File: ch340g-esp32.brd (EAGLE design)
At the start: 100 x 80 mm, 0 parts

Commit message: rev1
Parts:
- added C1, C2: 22, rcl:C0805
- added C3, C5: 0.1uF, rcl:C0805
- added C4: 10uF, rcl:B/3528-21W
- added D1: YELLOW, 597-5311-402F:LEDC2012X70N
- added D2: GREEN, 597-5311-402F:LEDC2012X70N
- added IC1: (no value), lm1117:SOT223
- added JP1: OUT, pinhead:1X06
- added Q1: 12M, crystal:HC49/S
- added R1, R2: 10K, rcl:R0805
- added R3, R4: 2K, rcl:R0805
- added T1, T2: BC847, transistor:SOT23
- added U$1: MICRO-USB, microusb:MICRO-USB
- added U$2: CH340G, ch340g:SOIC16
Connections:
- new net +5V: C3.1, IC1.3, U$1.1
- new net D+: U$1.3, U$2.5
- new net D-: U$1.2, U$2.6
- new net DTR: R1.1, T2.2, U$2.13
- new net EN: JP1.1, T1.3
- new net GND: C1.2, C2.2, C3.2, C4.-, C5.2, IC1.1, JP1.6, U$1.5, U$1.GND1, U$1.GND2, U$2.1
- new net IO0: JP1.2, T2.3
- new net N$1: C2.1, Q1.2, U$2.8
- new net N$12: D2.A, R4.1
- new net N$2: C1.1, Q1.1, U$2.7
- new net N$3: R1.2, T1.1
- new net N$4: R2.2, T2.1
- new net N$5: D1.A, R3.1
- new net RTS: R2.1, T1.2, U$2.14
- new net RX: D2.C, JP1.3, U$2.3
- new net TX: D1.C, JP1.4, U$2.2
- new net VCC: C4.+, C5.1, IC1.2, IC1.TAB, JP1.5, R3.2, R4.2, U$2.16, U$2.4
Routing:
- net GND: track 0.00 -> 113.3 mm, vias 0 -> 6
- net VCC: track 0.00 -> 64.0 mm, vias 0 -> 2
- net TX: track 0.00 -> 31.7 mm, vias 0 -> 1
- net RX: track 0.00 -> 25.2 mm
- net D+: track 0.00 -> 17.7 mm
- net RTS: track 0.00 -> 15.7 mm
- net D-: track 0.00 -> 14.4 mm
- net DTR: track 0.00 -> 13.9 mm, vias 0 -> 2
- net N$2: track 0.00 -> 11.3 mm
- net N$1: track 0.00 -> 10.9 mm
- net IO0: track 0.00 -> 10.7 mm
- net +5V: track 0.00 -> 7.46 mm
- net EN: track 0.00 -> 5.25 mm
- net N$4: track 0.00 -> 5.18 mm
- net N$3: track 0.00 -> 4.78 mm
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- added copper zone on layer 1, net GND
- added copper zone on layer 16, net GND
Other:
- board size 100 x 80 mm -> 22 x 43 mm
- board text added: "ESP32PRG"
- board text added: "RST BOOT RX TX 3.3V GND"

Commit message: board update
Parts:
- added D3: GREEN, 597-5311-402F:LEDC2012X70N
- added R5: 2K, rcl:R0805
- moved U$1 33.1 mm to (42.4, 10.8), turned to 90 degrees
- moved JP1 30.5 mm to (2.71, 10.9), turned to 90 degrees
- moved T1 29.0 mm to (8.00, 6.00), turned to 90 degrees
- moved IC1 28.2 mm to (32.0, 4.50), turned to 90 degrees
- moved C5 25.5 mm to (13.0, 6.00), turned to 180 degrees
- moved T2 25.5 mm to (8.00, 10.0), turned to 90 degrees
- moved C3 22.3 mm to (32.0, 9.50), turned to 180 degrees
- moved R2 22.0 mm to (13.0, 8.50), turned to 180 degrees
- moved D2 21.1 mm to (8.50, 13.5), turned to 0 degrees
- moved U$2 19.7 mm to (21.6, 8.12), turned to 90 degrees
- moved D1 19.2 mm to (8.50, 16.0), turned to 0 degrees
- moved R1 18.7 mm to (13.0, 11.0), turned to 180 degrees
- moved R4 15.6 mm to (13.0, 13.5), turned to 0 degrees
- moved R3 13.0 mm to (13.0, 16.0), turned to 0 degrees
- moved C4 8.00 mm to (13.0, 3.00), turned to 0 degrees
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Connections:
- new net N$6: D3.A, R5.1
- net GND: now also D3.C
- net VCC: now also R5.2
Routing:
- net GND: track 113.3 -> 0.00 mm, vias 6 -> 3
- net VCC: track 64.0 -> 76.0 mm
- net N$3: track 4.78 -> 11.9 mm
- net IO0: track 10.7 -> 5.46 mm
- net RTS: track 15.7 -> 12.0 mm
- net D+: track 17.7 -> 14.4 mm
- net N$6: track 0.00 -> 2.65 mm
- net RX: track 25.2 -> 27.8 mm, vias 0 -> 2
- net N$4: track 5.18 -> 3.17 mm
- net D-: track 14.4 -> 16.3 mm, vias 0 -> 2
- net N$2: track 11.3 -> 9.67 mm
- net N$5: track 3.92 -> 2.65 mm
- net N$12: track 3.86 -> 2.65 mm
- net DTR: track 13.9 -> 13.0 mm, vias 2 -> 0
- net TX: track 31.7 -> 31.1 mm
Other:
- board size 22 x 43 mm -> 43 x 22 mm

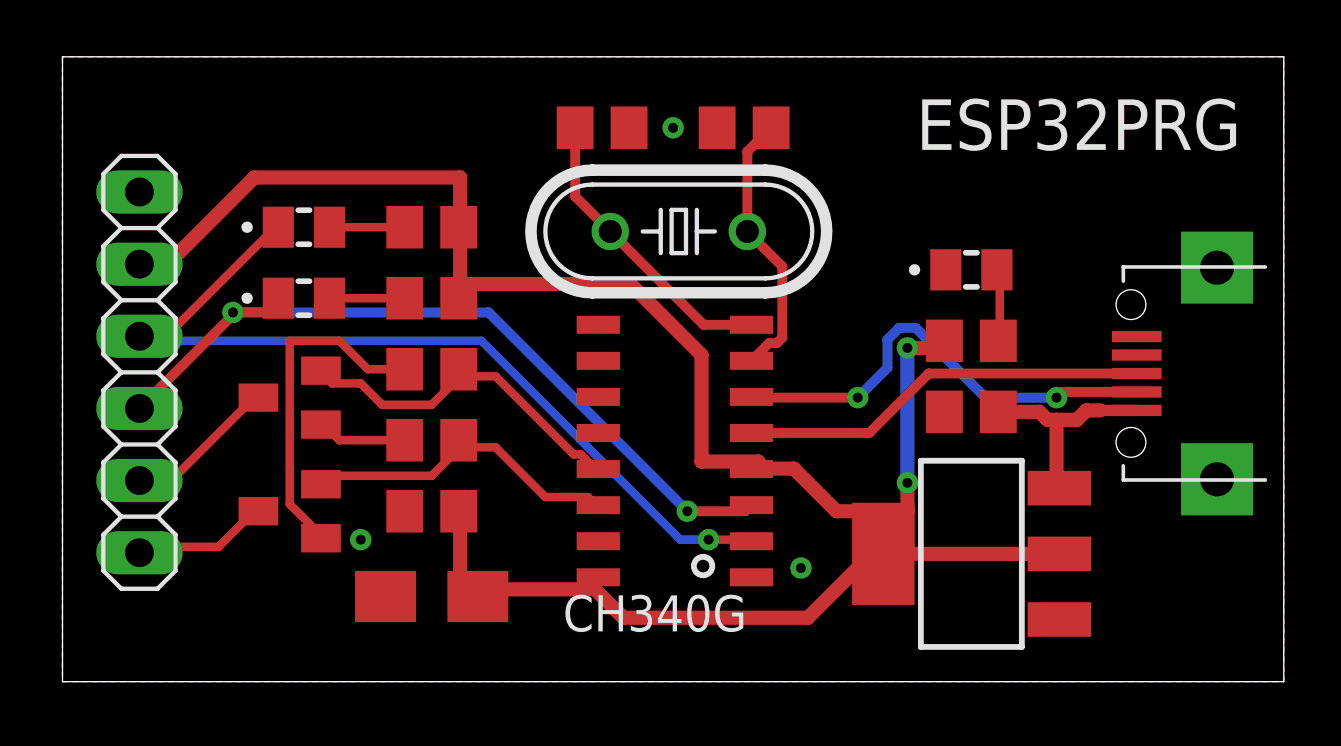
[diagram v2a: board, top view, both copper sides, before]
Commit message: USB TypeC connector; Smaller board
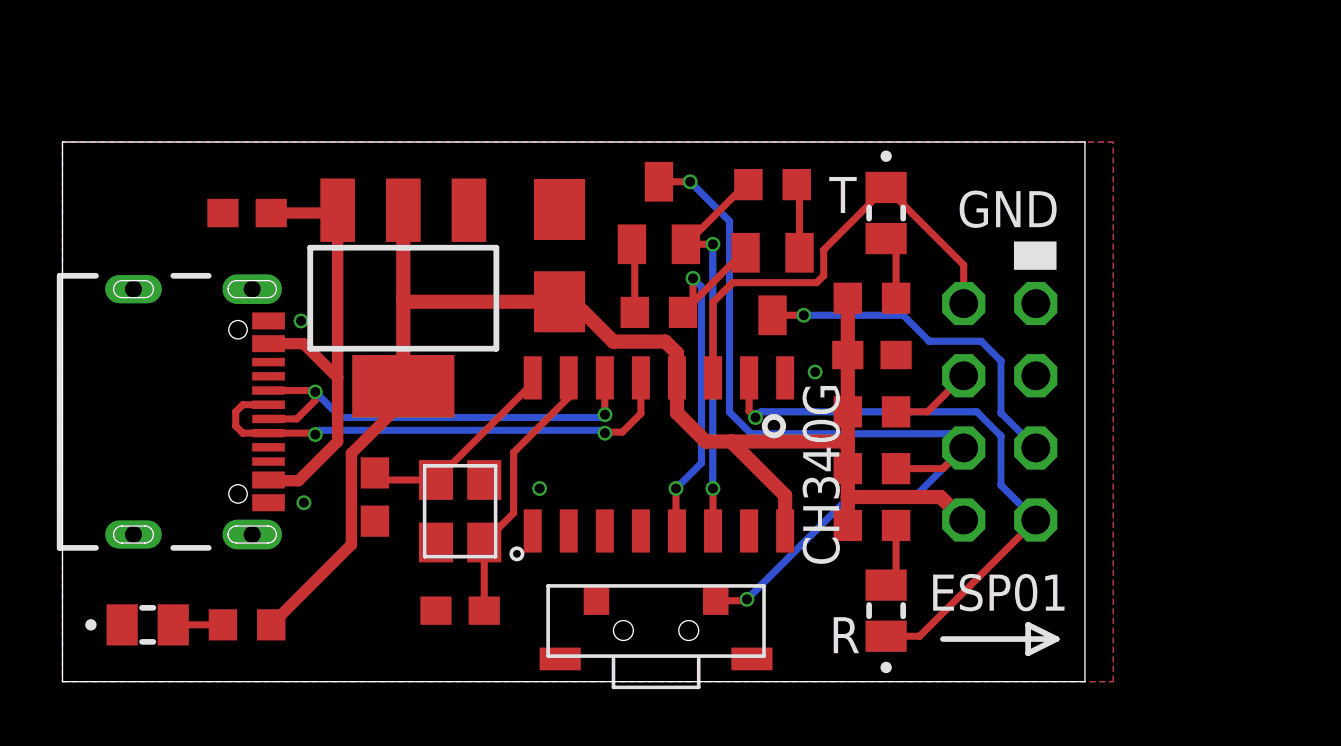
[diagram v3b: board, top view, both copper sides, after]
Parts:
- removed U$2: CH340G, ch340g:SOIC16
- added J1: USB4105_REVA, USB4105_REVA:GCT_USB4105_REVA
- added R6, R7: 10K, rcl:R0603
- added U1: CH340G, ch340g:SOIC16
- C1, C2, C3, C5: device rcl:C0805 -> rcl:C0603
- JP1: value OUT -> (none); device pinhead:1X06 -> pinhead:2X04
- Q1: value 12M -> 12MHz; device crystal:HC49/S -> crystal:SMD3225
- R1, R2: device rcl:R0805 -> rcl:R0603
- R3, R4, R5: value 2K -> 470; device rcl:R0805 -> rcl:R0603
- U$1: value MICRO-USB -> TS36CA-0.7; device microusb:MICRO-USB -> SMD Tact:SMD
- moved D3 31.6 mm to (3.00, 2.00)
- moved JP1 30.3 mm to (33.0, 9.50), flipped to the bottom, turned to 270 degrees
- moved R5 27.4 mm to (6.50, 2.00), turned to 0 degrees
- moved C3 26.4 mm to (6.50, 16.5)
- moved D1 24.5 mm to (29.0, 2.50), turned to 90 degrees
- moved U$1 23.3 mm to (20.9, 1.80), turned to 0 degrees
- moved IC1 21.9 mm to (12.0, 13.5), turned to 180 degrees
- moved D2 20.7 mm to (29.0, 16.5), turned to 270 degrees
- moved C1 19.7 mm to (14.0, 2.50)
- moved R3 18.7 mm to (28.5, 5.50), turned to 180 degrees
- moved T2 17.5 mm to (25.0, 14.0), turned to 180 degrees
- moved T1 16.7 mm to (21.0, 16.5), turned to 0 degrees
- moved C5 16.4 mm to (28.5, 11.5), turned to 0 degrees
- moved R4 15.5 mm to (28.5, 13.5), turned to 180 degrees
- moved C2 15.3 mm to (11.0, 6.50), turned to 270 degrees
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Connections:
- removed net +5V: C3.1, IC1.3, U$1.1
- removed net EN: JP1.1, T1.3
- removed net VCC: C4.+, C5.1, IC1.2, IC1.TAB, JP1.5, R3.2, R4.2, R5.2, U$2.16, U$2.4
- new net +3V3: C4.+, C5.1, IC1.2, IC1.TAB, JP1.8, R3.2, R4.2, R5.2, R6.2, R7.2, U1.16, U1.4
- new net CH_PD: JP1.4, R7.1
- new net IO2: JP1.3
- new net RST: JP1.6, R6.1, T1.3, U$1.D
- new net VBUS: C3.1, IC1.3, J1.A4/B9, J1.B4/A9
- net D+: now also J1.A6, J1.B6, U1.5; no longer U$1.3, U$2.5
- net D-: now also J1.A7, J1.B7, U1.6; no longer U$1.2, U$2.6
- net DTR: now also U1.13; no longer U$2.13
- net GND: now also J1.A1/B12, J1.B1/A12, J1.G1, J1.G2, J1.G3, J1.G4, JP1.1, Q1.P$2, Q1.P$4, U$1.A, U$1.B, U$1.C, U1.1; no longer JP1.6, U$1.5, U$1.GND1, U$1.GND2, U$2.1
- net IO0: now also JP1.5; no longer JP1.2
- net N$1: now also Q1.P$3, U1.8; no longer Q1.2, U$2.8
- net N$2: now also Q1.P$1, U1.7; no longer Q1.1, U$2.7
- net RTS: now also U1.14; no longer U$2.14
- net RX: now also JP1.2, U1.3; no longer JP1.3, U$2.3
- net TX: now also JP1.7, U1.2; no longer JP1.4, U$2.2
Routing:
- net VCC: track 76.0 -> 0.00 mm, vias 2 -> 0
- net +3V3: track 0.00 -> 51.8 mm
- net RST: track 0.00 -> 32.2 mm, vias 0 -> 2
- net VBUS: track 0.00 -> 16.5 mm
- net RX: track 27.8 -> 16.2 mm, vias 2 -> 0
- net TX: track 31.1 -> 21.0 mm
- net N$3: track 11.9 -> 2.44 mm
- net +5V: track 7.69 -> 0.00 mm
- net IO0: track 5.46 -> 12.3 mm, vias 0 -> 1
- net EN: track 4.88 -> 0.00 mm
- net D+: track 14.4 -> 17.8 mm, vias 0 -> 2
- net N$1: track 10.5 -> 7.26 mm
- net CH_PD: track 0.00 -> 2.91 mm
- net RTS: track 12.0 -> 14.1 mm, vias 0 -> 2
- net N$6: track 2.65 -> 1.75 mm
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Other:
- board size 43 x 22 mm -> 36 x 19 mm
- board text added: "3.3V"
- board text added: "Andrey Ovcharov"
- board text added: "CH_PD"
- board text added: "Designed by"
- board text added: "ESP01"
- board text added: "ESP32"
- board text added: "ESP8266"
- board text added: "GND"
- board text added: "IO0"
- board text added: "IO2"
- board text added: "R"
- board text added: "RST"
- board text added: "RX"
- board text added: "T"
- board text added: "TX"
- board text added: "USB-UART"
- board text added: "https://ovcharov.me/"
- board text removed: "ESP32PRG"
- board text removed: "RST BOOT RX TX 3.3V GND"

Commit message: Production files
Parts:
- C3, C5: value 0.1uF -> 10u
- C4: value 10uF -> 100u
- D1: value YELLOW -> BLUE
- D2: value GREEN -> BLUE
- moved C1 1.58 mm to (13.5, 4.00)
- moved C2 1.58 mm to (10.5, 8.00)
- moved Q1 1.58 mm to (13.5, 7.50)
- moved C4 1.12 mm to (17.0, 16.0)
- moved D2 1.00 mm to (29.0, 17.5)
- moved D3 1.00 mm to (3.00, 3.00)
- moved IC1 1.00 mm to (12.0, 14.5)
- moved R5 1.00 mm to (6.50, 3.00)
- moved C3 0.50 mm to (6.50, 17.0)
- moved C5 0.50 mm to (28.5, 12.0)
- moved J1 0.50 mm to (2.50, 10.0)
- moved JP1 0.50 mm to (33.0, 10.0)
- moved R1 0.50 mm to (21.0, 13.5)
- moved R2 0.50 mm to (25.0, 18.0)
- moved R3 0.50 mm to (28.5, 6.00)
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- renumbered U$1 to BTN1
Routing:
- net +3V3: track 51.8 -> 58.4 mm, vias 0 -> 3
- net RTS: track 14.1 -> 16.9 mm, vias 2 -> 0
- net DTR: track 13.8 -> 11.6 mm, vias 2 -> 0
- net RX: track 16.2 -> 17.8 mm, vias 0 -> 1
- net IO0: track 12.3 -> 13.9 mm, vias 1 -> 0
- net D+: track 17.8 -> 16.5 mm
- net RST: track 32.2 -> 31.3 mm
- net D-: track 15.8 -> 16.5 mm
- net N$2: track 9.43 -> 8.87 mm
- net N$5: track 2.24 -> 2.79 mm
- net N$12: track 2.24 -> 2.74 mm
- net TX: vias 1 -> 0
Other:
- board size 36 x 19 mm -> 36 x 20 mm
- board text added: "JLCJLCJLCJLC"
- board text added: "On"
- board text added: "Reset"
- board text removed: "ESP32"
- board text removed: "ESP8266"
